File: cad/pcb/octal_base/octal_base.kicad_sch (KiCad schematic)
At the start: 13 parts, among them J1 Octal Base, J2 Pin Socket

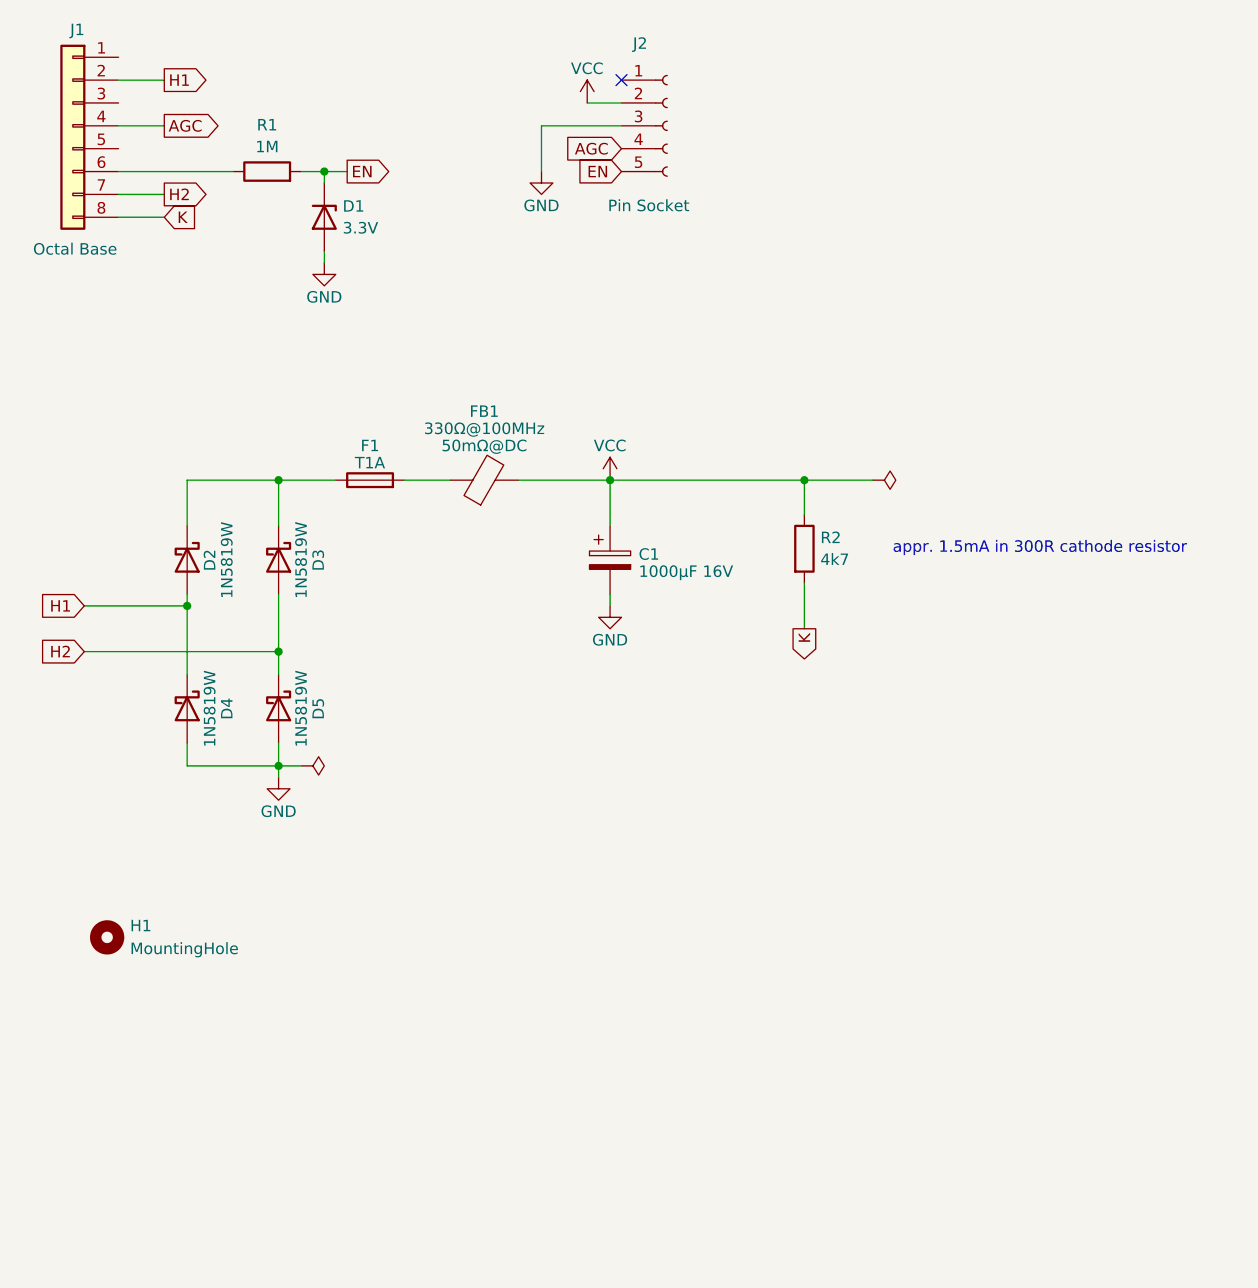
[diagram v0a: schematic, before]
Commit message: Fix: EM34 socket, don't use bridge rect...
gnd floats at approx. 1/2 vcc relative to chassis-gnd -- oops.
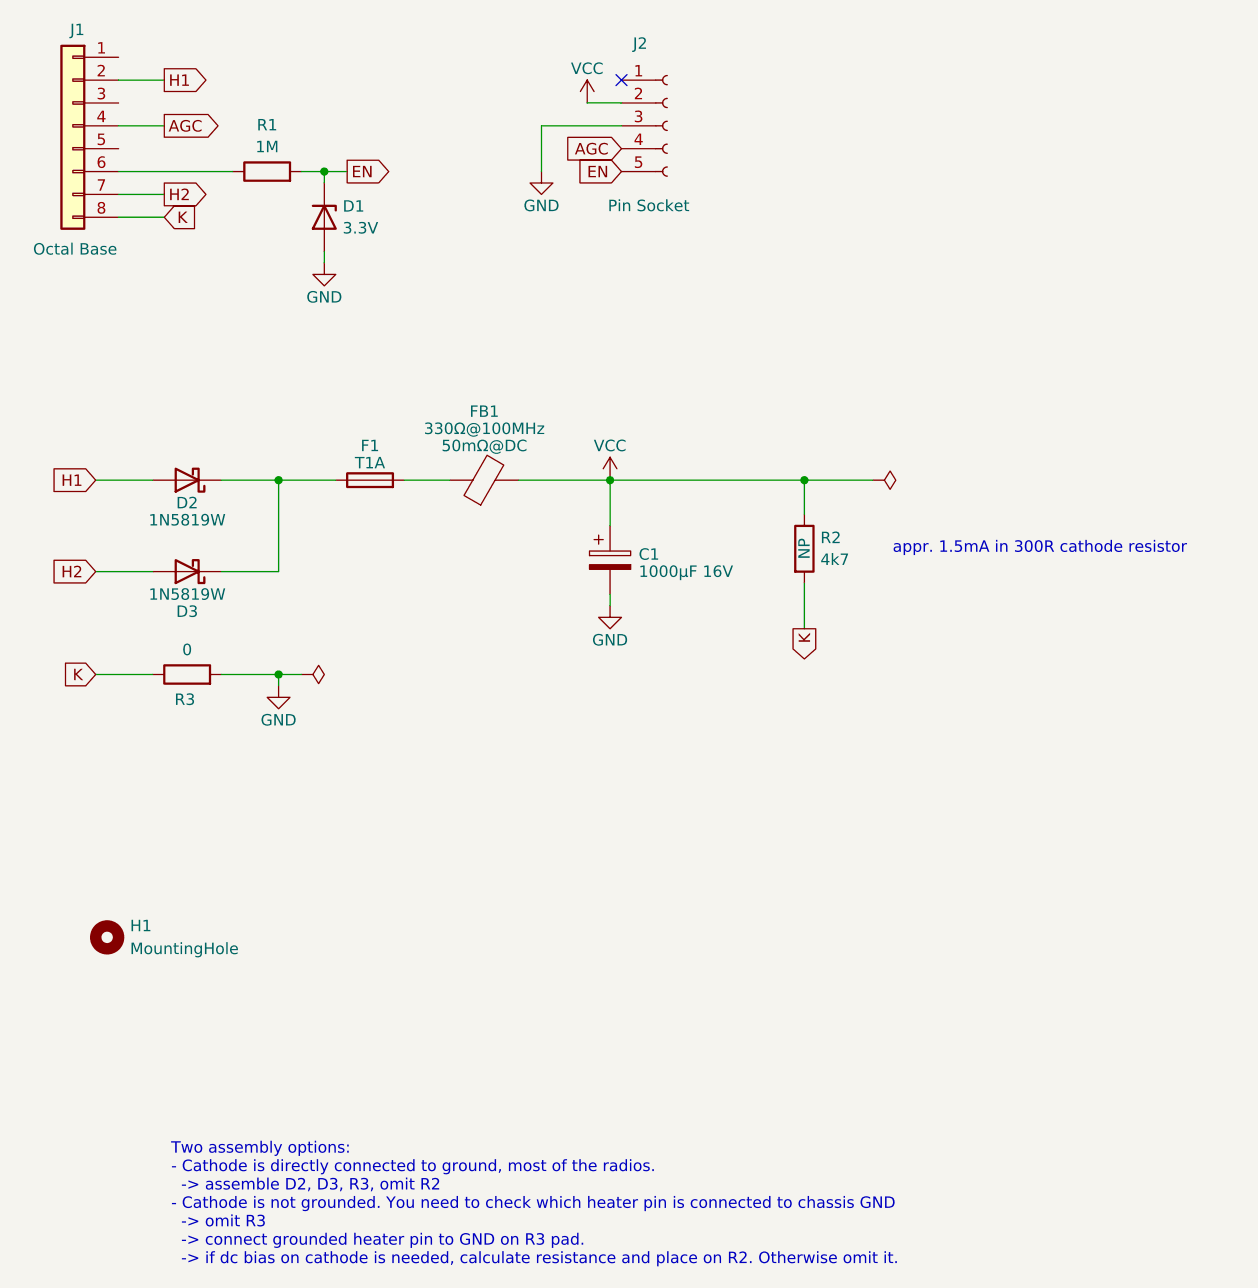
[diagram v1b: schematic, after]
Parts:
- removed D4, D5: 1N5819W, D_SOD-323_HandSoldering, symbol Diode:1N5819WS
- added R3: 0, Resistor_SMD:R_0603_1608Metric_Pad0.98x0.95mm_HandSolder, symbol Device:R
- R2: Placement (none) -> NP
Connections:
- net GND: now also R3.2
- net K: now also R3.1
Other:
- note added: "Two assembly options: - Cathode is directly connected to ground, most of the radios. -> assemble D2, D3, R3, omit R2 - Cathode is not grounded. You need to check which heater pin is connected to chassis GND -> omit R3 -> connect grounded heater pin to GND on R3 pad. -> if dc bias on cathode is needed, calculate resistance and place on R2. Otherwise omit it."
- moved on the sheet: D2, D3
